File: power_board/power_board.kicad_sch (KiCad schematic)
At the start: 1 part, among them U1 STM32L431KCUx

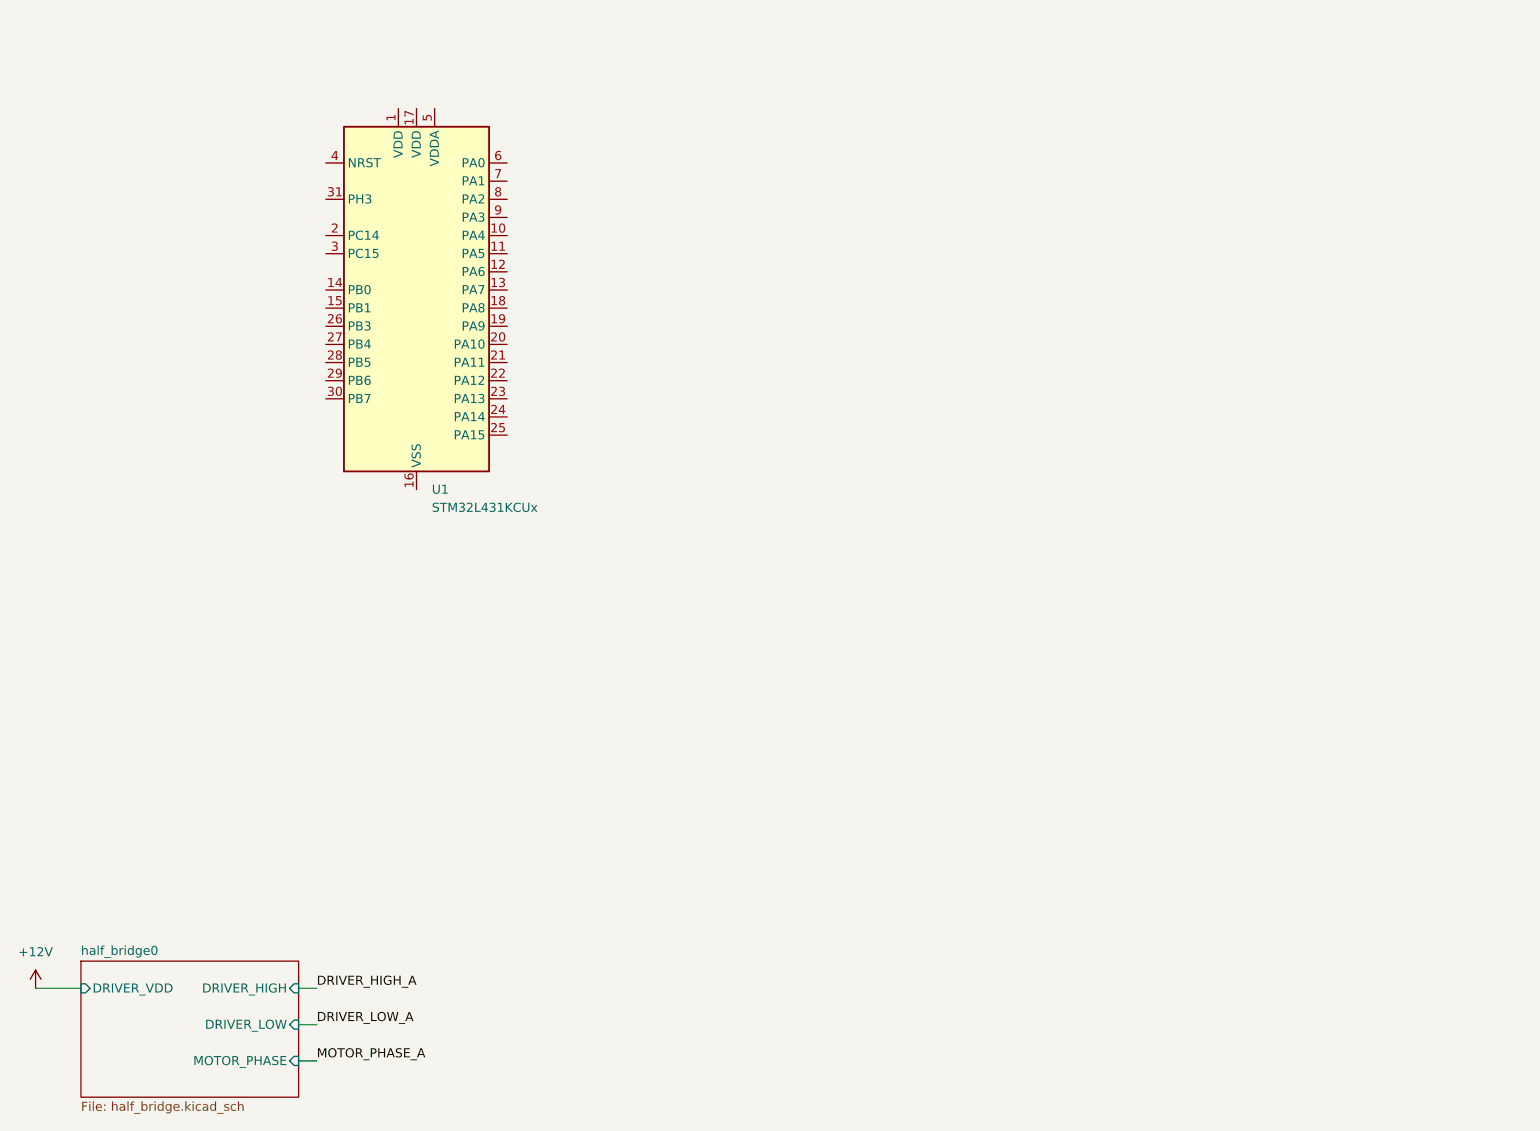
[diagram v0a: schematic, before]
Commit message: Seperat submodules into split sheets
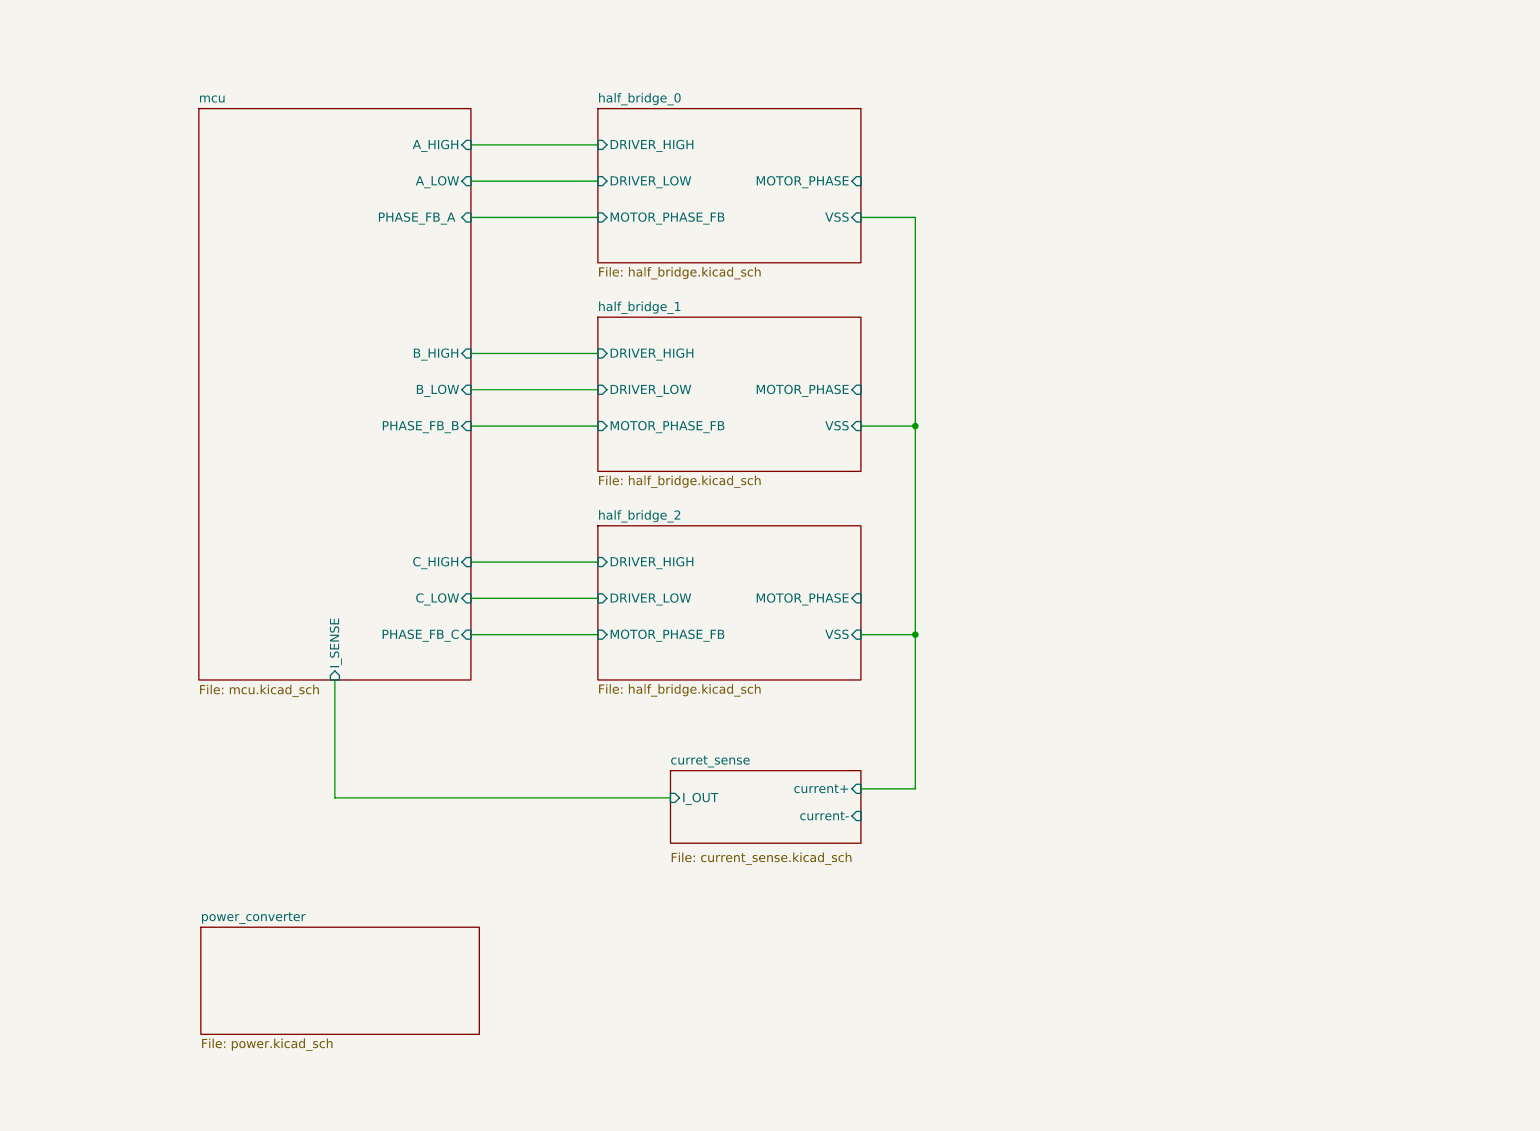
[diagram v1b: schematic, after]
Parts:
- removed U1: STM32L431KCUx, Package_DFN_QFN:QFN-32-1EP_5x5mm_P0.5mm_EP3.1x3.1mm_ThermalVias, symbol MCU_ST_STM32L4:STM32L431KCUx
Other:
- sheet half_bridge0 renamed half_bridge_0
- added sheet curret_sense (current_sense.kicad_sch)
- added sheet half_bridge_1 (half_bridge.kicad_sch)
- added sheet half_bridge_2 (half_bridge.kicad_sch)
- added sheet mcu (mcu.kicad_sch)
- added sheet power_converter (power.kicad_sch)
- sheet half_bridge_0 ports: added MOTOR_PHASE_FB, VSS; removed DRIVER_VDD

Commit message: Complete sch design without check
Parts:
- added C32, C33, C34, C35: C_Small, Capacitor_SMD:C_2220_5750Metric, symbol Device:C_Small
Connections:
- new net GND: C32.2, C33.2, C34.2, C35.2
- new net VBUS: C32.1, C33.1, C34.1, C35.1
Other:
- sheet half_bridge_0 ports: added VDD; removed none
- sheet half_bridge_1 ports: added VDD; removed none
- sheet half_bridge_2 ports: added VDD; removed none

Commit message: Start multichannel layout
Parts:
- C1: renamed from C32; value C_Small -> 10u
- C2: renamed from C33; value C_Small -> 10u
- C3: renamed from C34; value C_Small -> 10u
- C4: renamed from C35; value C_Small -> 10u
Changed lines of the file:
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@@
 		(dnp no)
 		(fields_autoplaced yes)
-		(property "Reference" "#PWR048"
+		(property "Reference" "#PWR03"
 			(at 167.64 48.26 0)
 			(effects
@@
 			(project ""
 				(path "/c786dd1f-c97f-4c1e-a27a-ac5828b3c50c"
-					(reference "#PWR048")
+					(reference "#PWR03")
 					(unit 1)
 				)
@@
 		(on_board yes)
 		(dnp no)
-		(property "Reference" "C33"
+		(property "Reference" "C2"
 			(at 152.908 35.814 90)
 			(effects
@@
 			)
 		)
-		(property "Value" "C_Small"
+		(property "Value" "10u"
 			(at 155.448 35.814 90)
 			(effects
@@
 			(project "power_board"
 				(path "/c786dd1f-c97f-4c1e-a27a-ac5828b3c50c"
-					(reference "C33")
+					(reference "C2")
 					(unit 1)
 				)
@@
 		(on_board yes)
 		(dnp no)
-		(property "Reference" "C32"
+		(property "Reference" "C1"
 			(at 146.558 35.814 90)
 			(effects
@@
 			)
 		)
-		(property "Value" "C_Small"
+		(property "Value" "10u"
 			(at 149.098 35.814 90)
 			(effects
@@
 			(project ""
 				(path "/c786dd1f-c97f-4c1e-a27a-ac5828b3c50c"
-					(reference "C32")
+					(reference "C1")
 					(unit 1)
 				)
@@
 		(on_board yes)
 		(dnp no)
-		(property "Reference" "C34"
+		(property "Reference" "C3"
 			(at 159.258 35.814 90)
 			(effects
@@
 			)
 		)
-		(property "Value" "C_Small"
+		(property "Value" "10u"
 			(at 161.798 35.814 90)
 			(effects
@@
 			(project "power_board"
 				(path "/c786dd1f-c97f-4c1e-a27a-ac5828b3c50c"
-					(reference "C34")
+					(reference "C3")
 					(unit 1)
 				)
@@
 		(on_board yes)
 		(dnp no)
-		(property "Reference" "C35"
+		(property "Reference" "C4"
 			(at 165.608 35.814 90)
 			(effects
@@
 			)
 		)
-		(property "Value" "C_Small"
+		(property "Value" "10u"
 			(at 168.148 35.814 90)
 			(effects
@@
 			(project "power_board"
 				(path "/c786dd1f-c97f-4c1e-a27a-ac5828b3c50c"
-					(reference "C35")
+					(reference "C4")
 					(unit 1)
 				)
@@
 		(dnp no)
 		(fields_autoplaced yes)
-		(property "Reference" "#PWR049"
+		(property "Reference" "#PWR02"
 			(at 146.05 162.56 0)
 			(effects
@@
 			(project "power_board"
 				(path "/c786dd1f-c97f-4c1e-a27a-ac5828b3c50c"
-					(reference "#PWR049")
+					(reference "#PWR02")
 					(unit 1)
 				)
@@
 		(dnp no)
 		(fields_autoplaced yes)
-		(property "Reference" "#PWR047"
+		(property "Reference" "#PWR01"
 			(at 142.24 38.1 0)
 			(effects
@@
 			(project ""
 				(path "/c786dd1f-c97f-4c1e-a27a-ac5828b3c50c"
-					(reference "#PWR047")
-					(unit 1)
-				)
+					(reference "#PWR01")
+					(unit 1)
+				)

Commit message: Complete primary layout step
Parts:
- removed C1, C2, C3, C4: 10u, Capacitor_SMD:C_2220_5750Metric, symbol Device:C_Small
- added C37, C38: ERS1KM101G16OT, esc-library:CAP-TH_BD10.0-P5.00-D1.0-FD, symbol esc-library:ERS1KM101G16OT
- added CN1: XT90PW-M.G.Y, esc-library:CONN-TH_XT90PW-M.G.Y, symbol esc-library:XT90PW-M.G.Y
- added CN2: XT60PW-M, esc-library:CONN-TH_XT60PW-M, symbol esc-library:XT60PW-M
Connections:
- net GNDPWR: now also CN1.1 (-), CN1.3, CN1.4, CN2.1 (-), CN2.3, CN2.4
- net VBUS: now also C37.1, C38.1, CN1.2 (+), CN2.2 (+)
- net curret_sense/current+: now also C37.2, C38.2

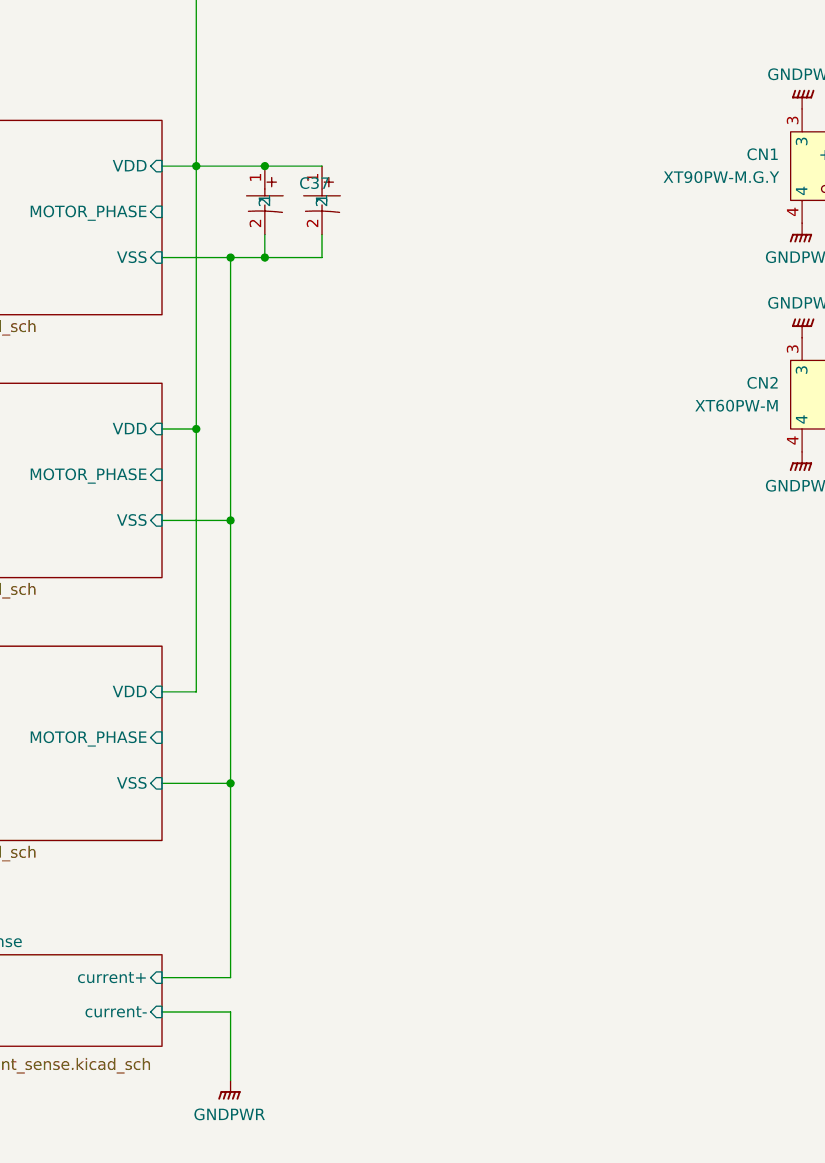
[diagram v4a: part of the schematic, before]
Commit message: Complete layout, and copper zone design
TODO!!!: move DCDC zone from GND area to PGND(current+)
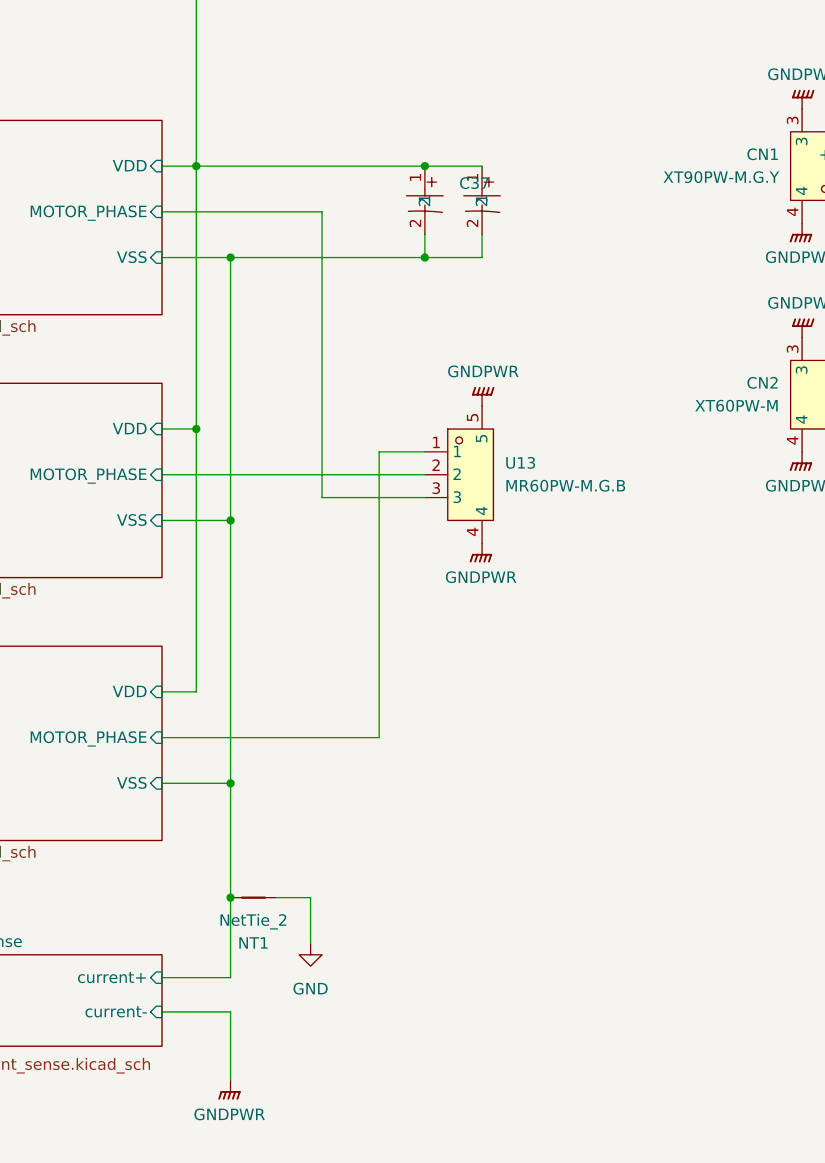
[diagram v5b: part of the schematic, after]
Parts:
- added NT1: NetTie_2, NetTie:NetTie-2_SMD_Pad2.0mm, symbol Device:NetTie_2
- added U13: MR60PW-M.G.B, esc-library:CONN-TH_MR60PW, symbol esc-library:MR60PW-M.G.B
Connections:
- net GNDPWR: now also U13.4, U13.5
- net curret_sense/current+: now also NT1.2
- net half_bridge_0/MOTOR_PHASE: now also U13.3
- net half_bridge_1/MOTOR_PHASE: now also U13.2
- net half_bridge_2/MOTOR_PHASE: now also U13.1
- new net GND: NT1.1
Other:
- moved on the sheet: C37

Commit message: All drc error solved
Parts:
- NT1: footprint NetTie:NetTie-2_SMD_Pad2.0mm -> NetTie:NetTie-2_THT_Pad0.3mm
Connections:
- net GNDPWR: no longer CN1.3, CN1.4, CN2.3, CN2.4, U13.4, U13.5
- no-connect marks 0 -> 6
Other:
- sheet power_converter ports: added VSS; removed none
